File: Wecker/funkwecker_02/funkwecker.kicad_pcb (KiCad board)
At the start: 2 copper layers, 115.1 x 72 mm, 20 parts, among them J1 DCF77-Connector, J2 Debug-Interface, J3 LED-Display Connector (TM1637), SW1 Hauptschalter, U1 MCP1702-3302, U2 STM8L051F3P, U8 MCP1702-5002, Y1 HC49U 16MHz

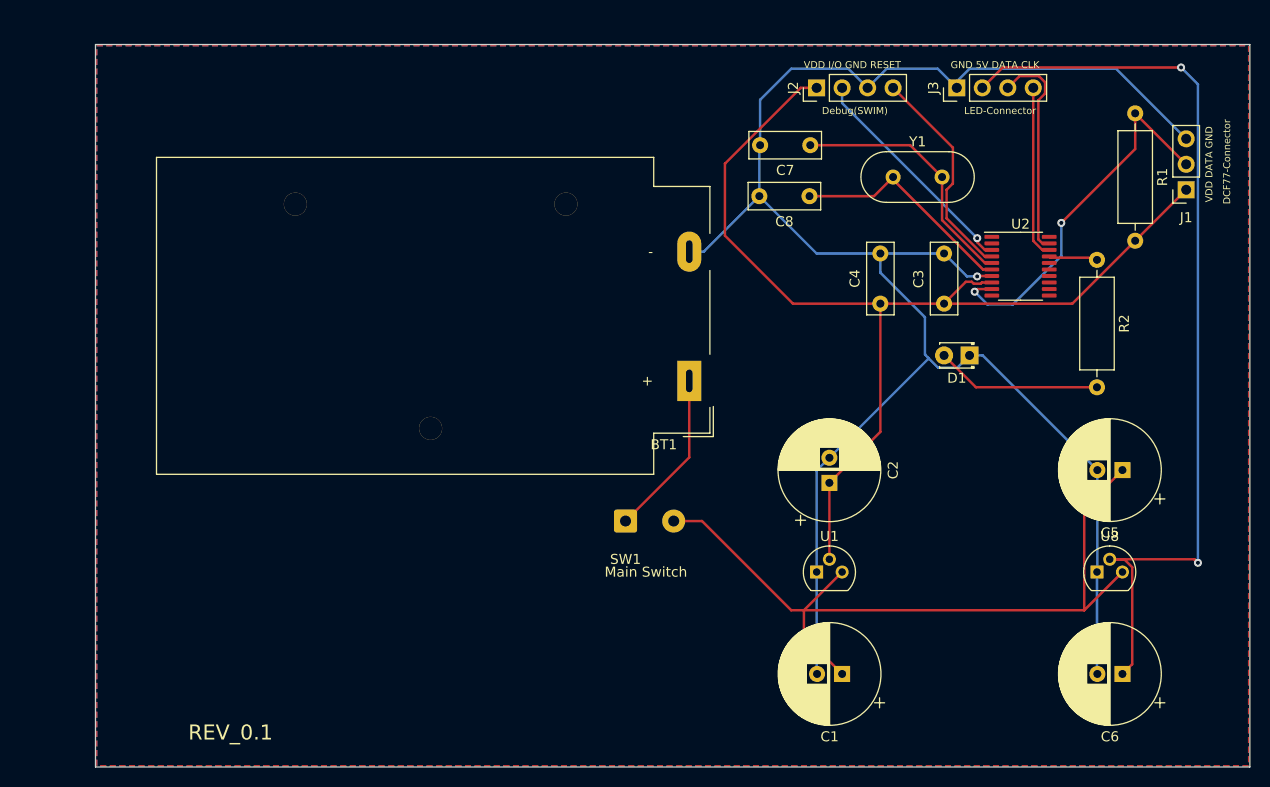
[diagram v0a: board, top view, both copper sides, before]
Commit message: Rev 2: Fehler korrigiert und neue Anordnung
Fehler:
-Fehlender Kondensator am RESET-Pin
-Fehlerhaftes Layout für beide Spannungsregler korrigiert
-Benötigten Platz verringert
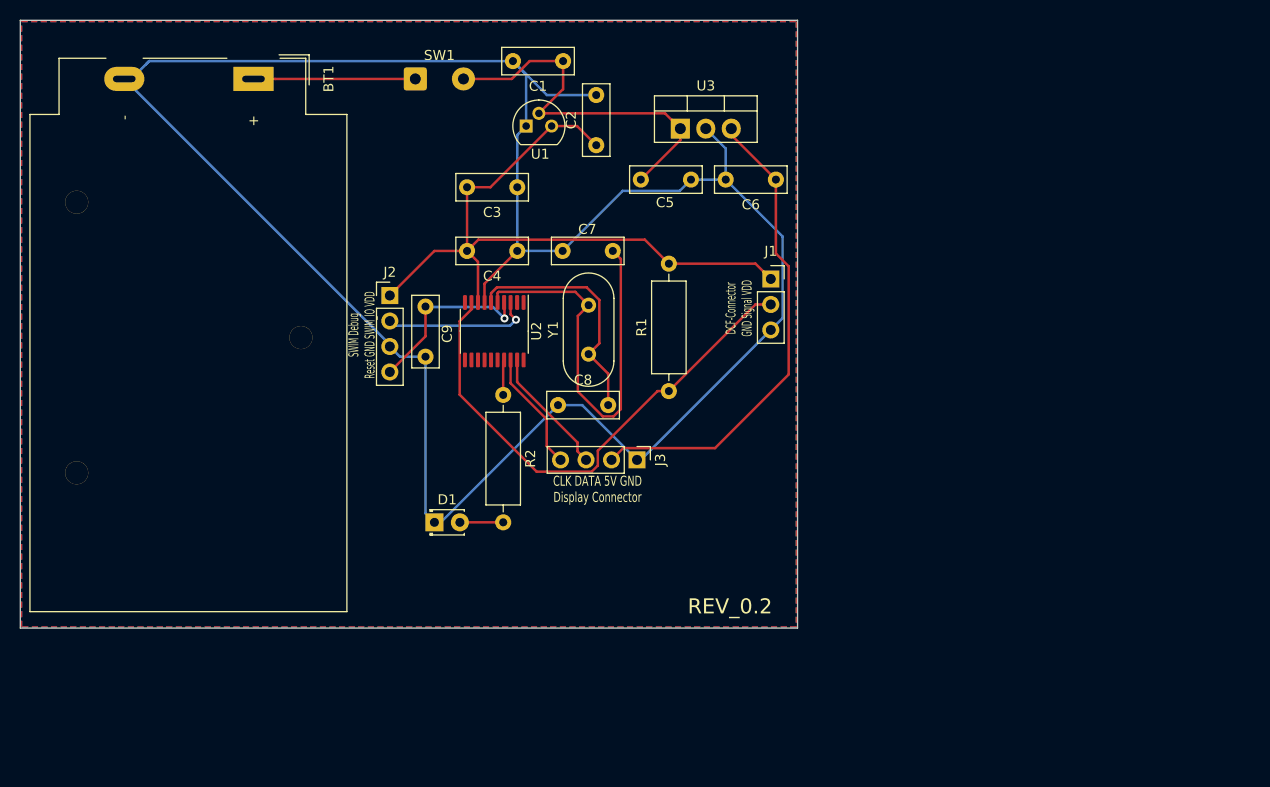
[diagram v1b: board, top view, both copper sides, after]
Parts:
- removed U8: MCP1702-5002, Package_TO_SOT_THT:TO-92
- added C9: 100nF, Capacitor_THT:C_Disc_D7.0mm_W2.5mm_P5.00mm, F.Cu at (116.7, 84.5)
- added U3: L7805, Package_TO_SOT_THT:TO-220-3_Vertical, F.Cu at (142.1, 61.7)
- C1, C2: footprint Capacitor_THT:CP_Radial_D10.0mm_P2.50mm -> Capacitor_THT:C_Disc_D7.0mm_W2.5mm_P5.00mm
- C5: value 1µF -> 0.33µF; footprint Capacitor_THT:CP_Radial_D10.0mm_P2.50mm -> Capacitor_THT:C_Disc_D7.0mm_W2.5mm_P5.00mm
- C6: value 1µF -> 0.1µF; footprint Capacitor_THT:CP_Radial_D10.0mm_P2.50mm -> Capacitor_THT:C_Disc_D7.0mm_W2.5mm_P5.00mm
- R2: value 330 -> 1k
- moved C1 67.1 mm to (130.4, 55.0)
- moved R2 60.7 mm to (124.5, 88.3)
- moved C6 60.2 mm to (151.6, 66.8)
- moved C5 56.1 mm to (138.2, 66.8), turned to 0 degrees
- moved D1 55.9 mm to (117.6, 101.0), turned to 0 degrees
- moved R1 54.1 mm to (141.0, 87.9), turned to 90 degrees
- moved U1 53.0 mm to (126.7, 61.5)
- moved U2 52.8 mm to (123.6, 81.9), turned to 270 degrees
- moved BT1 52.8 mm to (99.6, 56.8), turned to 270 degrees
- moved J3 48.9 mm to (137.8, 94.7), turned to 270 degrees
- moved SW1 48.8 mm to (115.7, 56.8)
- moved J2 47.3 mm to (113.2, 78.4), turned to 0 degrees
- moved C3 43.1 mm to (125.9, 67.6), turned to 180 degrees
- moved J1 42.3 mm to (151.1, 76.7), turned to 0 degrees
- moved C2 40.9 mm to (133.7, 63.4)
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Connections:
- U1 pad 2: VDD -> VCC
- U1 pad 3: VCC -> VDD
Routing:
- net +5V: track 93.3 -> 48.1 mm, vias 2 -> 0
- net GND: track 186.9 -> 227.9 mm, vias 1 -> 0
- net VCC: track 78.9 -> 38.3 mm
- net VDD: track 106.3 -> 70.0 mm
- net OSC_IN: track 25.5 -> 41.8 mm
- net DCF_SIGNAL: track 37.4 -> 51.6 mm, vias 2 -> 0
- net Net-(D1-Pad2): track 16.6 -> 4.32 mm
- net LED_DISPLAY_DATA: track 21.7 -> 12.8 mm
- net SWIM_I_O: track 22.8 -> 15.0 mm
- net LED_DISPLAY_CLK: track 17.2 -> 12.0 mm
- net RESET: track 21.8 -> 18.0 mm, vias 0 -> 1
- net Test_LED: track 4.91 -> 3.52 mm
- net OSC_OUT: track 22.9 -> 24.2 mm
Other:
- board size 115.1 x 72 mm -> 77.5 x 60.6 mm
- board text added: "CLK DATA 5V GND Display Connector"
- board text added: "DCF-Connector GND Signal VDD"
- board text added: "REV_0.2"
- board text added: "SWIM Debug Reset GND SWIM_IO VDD"
- board text removed: "DCF77-Connector"
- board text removed: "Debug(SWIM)"
- board text removed: "GND 5V DATA CLK"
- board text removed: "LED-Connector"
- board text removed: "Main Switch"
- board text removed: "REV_0.1"
- board text removed: "VDD DATA GND"
- board text removed: "VDD I/O GND RESET"
